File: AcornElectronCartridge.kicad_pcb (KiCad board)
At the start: 2 copper layers, 84.9 x 62.5 mm, 5 parts

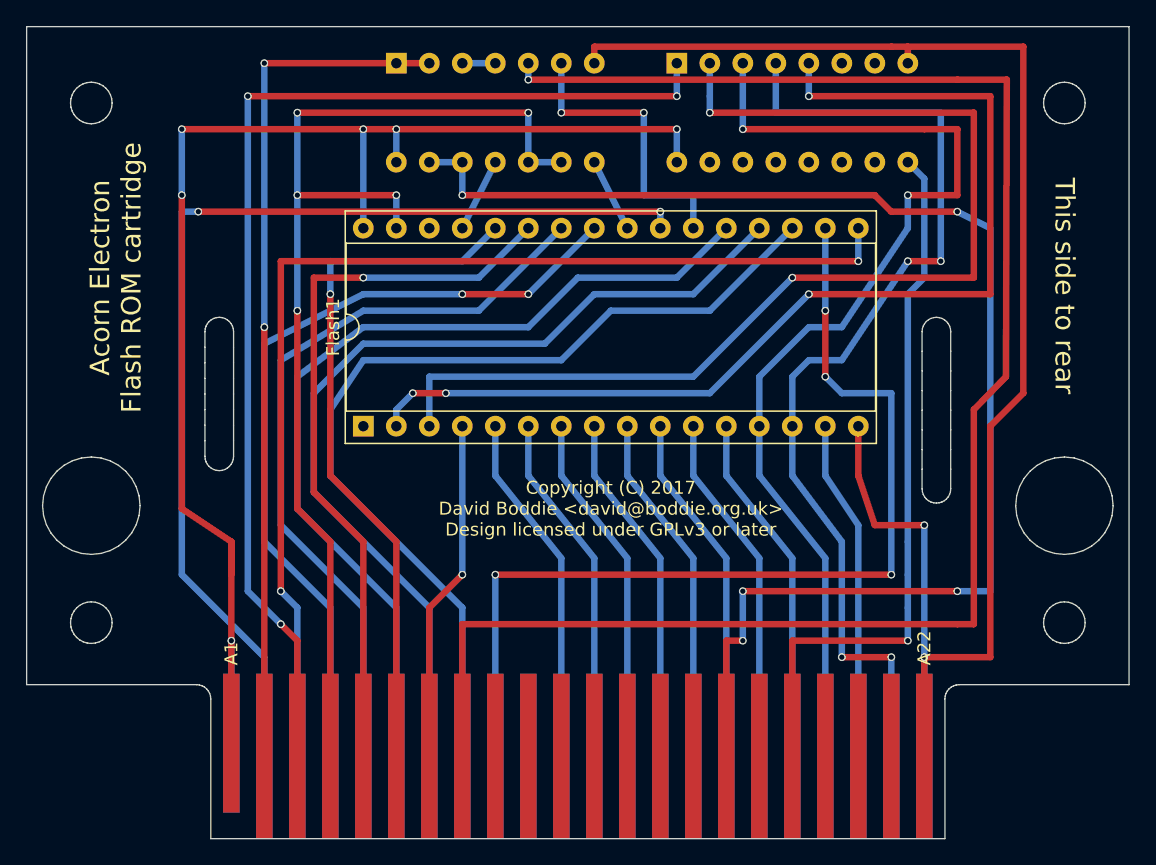
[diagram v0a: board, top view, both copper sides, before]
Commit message: Tidied up tracks to leave more space between silkscreen markings and vias. Only used one +5V line and kept the 0V lines separate.
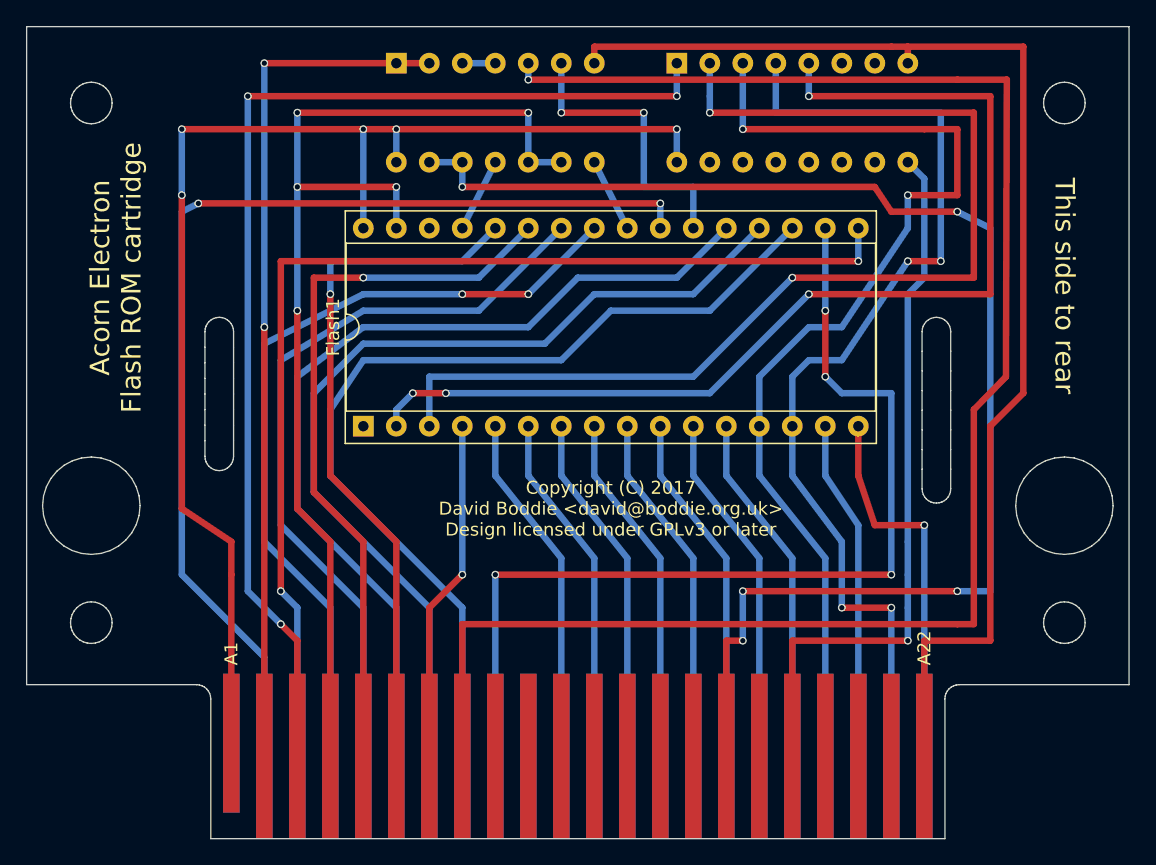
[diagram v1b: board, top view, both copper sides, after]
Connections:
- CONN2 pad 1: VCC -> /+5V_B
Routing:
- net VCC: track 110.5 -> 100.1 mm, vias 6 -> 5
- net /A10: track 82.6 -> 83.4 mm
- net /CSRW: track 84.9 -> 85.5 mm
- net GND: vias 2 -> 1

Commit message: Placed all tracks linked to flash ROM pads on the same side of the board.
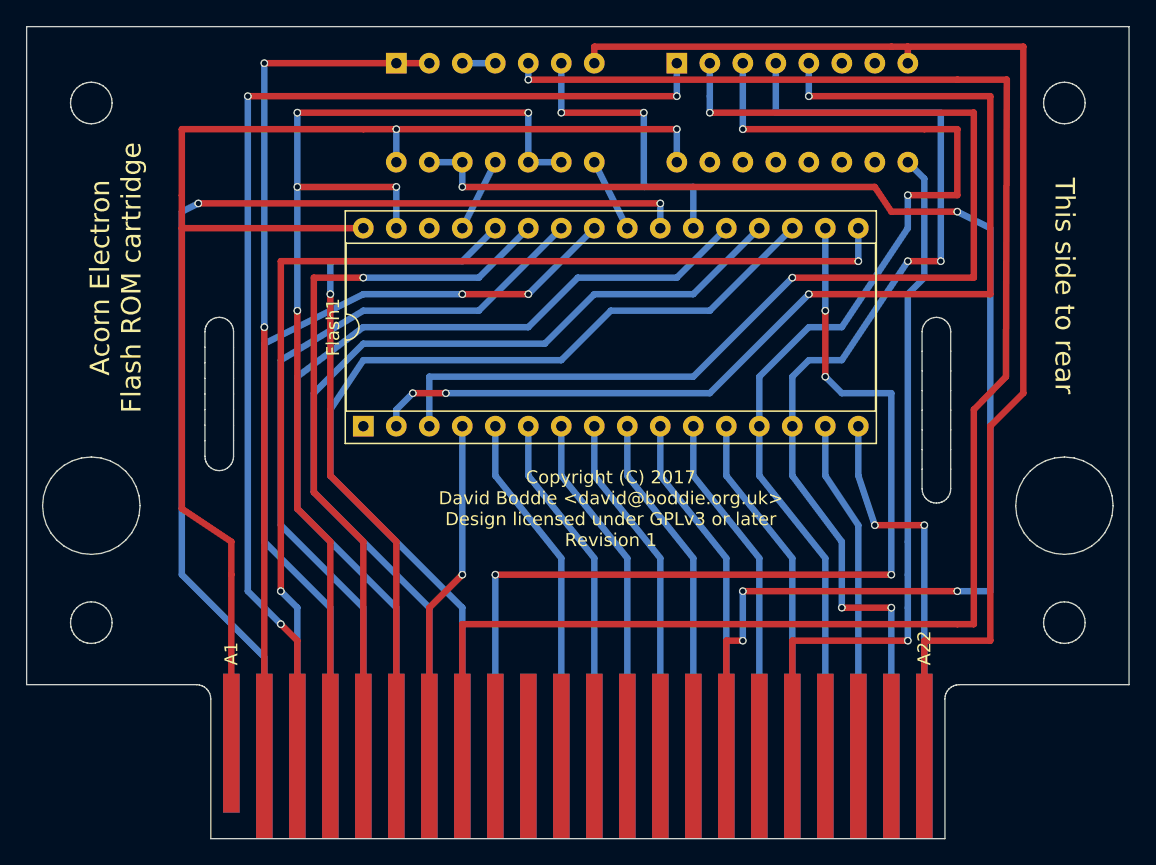
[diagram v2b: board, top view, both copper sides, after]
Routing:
- net VCC: track 100.1 -> 106.4 mm, vias 5 -> 2
- net GND: vias 1 -> 2
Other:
- board text added: "Copyright (C) 2017 David Boddie <david@boddie.org.uk> Design licensed under GPLv3 or later Revision 1"
- board text removed: "Copyright (C) 2017 David Boddie <david@boddie.org.uk> Design licensed under GPLv3 or later"
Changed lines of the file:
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@@
     (thickness 1.6)
     (drawings 322)
-    (tracks 295)
+    (tracks 294)
     (zones 0)
     (modules 5)
@@
     )
   )
-  (gr_text "Copyright (C) 2017\nDavid Boddie <david@boddie.org.uk>\nDesign licensed under GPLv3 or later" (at 105.41 101.6) (layer F.SilkS)
+  (gr_text "Copyright (C) 2017\nDavid Boddie <david@boddie.org.uk>\nDesign licensed under GPLv3 or later\nRevision 1" (at 105.41 101.6) (layer F.SilkS)
     (effects (font (size 1 1) (thickness 0.15)))
   )
@@
   (segment (start 119.38 99.06) (end 119.38 99.06) (width 0.5) (layer B.Cu) (net 39))
   (segment (start 119.38 99.06) (end 119.38 95.25) (width 0.5) (layer B.Cu) (net 39) (status 20))
+  (segment (start 86.36 80.01) (end 72.39 80.01) (width 0.5) (layer F.Cu) (net 41))
+  (segment (start 72.39 77.47) (end 72.39 72.39) (width 0.5) (layer F.Cu) (net 41))
+  (segment (start 86.36 72.39) (end 72.39 72.39) (width 0.5) (layer F.Cu) (net 41))
+  (segment (start 76.2 104.14) (end 72.39 101.6) (width 0.5) (layer F.Cu) (net 41))
+  (segment (start 72.39 101.6) (end 72.39 80.01) (width 0.5) (layer F.Cu) (net 41))
+  (segment (start 72.39 80.01) (end 72.39 77.47) (width 0.5) (layer F.Cu) (net 41))
+  (segment (start 76.2 104.14) (end 76.2 106.68) (width 0.5) (layer F.Cu) (net 41))
+  (segment (start 76.2 106.68) (end 76.2 119.65) (width 0.5) (layer F.Cu) (net 41))
   (segment (start 110.49 74.93) (end 110.49 72.39) (width 0.5) (layer B.Cu) (net 41) (status 10))
   (segment (start 110.49 72.39) (end 88.9 72.39) (width 0.5) (layer F.Cu) (net 41))
@@
   (segment (start 86.36 72.39) (end 88.9 72.39) (width 0.5) (layer F.Cu) (net 41))
   (segment (start 88.9 72.39) (end 88.9 74.93) (width 0.5) (layer B.Cu) (net 41) (status 20))
-  (via (at 72.39 77.47) (size 0.6) (drill 0.4) (layers F.Cu B.Cu) (net 41))
-  (segment (start 76.2 104.14) (end 72.39 101.6) (width 0.5) (layer F.Cu) (net 41))
-  (segment (start 72.39 101.6) (end 72.39 77.47) (width 0.5) (layer F.Cu) (net 41))
-  (segment (start 72.39 72.39) (end 86.36 72.39) (width 0.5) (layer F.Cu) (net 41))
-  (via (at 72.39 72.39) (size 0.6) (drill 0.4) (layers F.Cu B.Cu) (net 41))
-  (segment (start 72.39 77.47) (end 72.39 72.39) (width 0.5) (layer B.Cu) (net 41))
-  (segment (start 86.36 72.39) (end 86.36 80.01) (width 0.5) (layer B.Cu) (net 41) (status 20))
-  (segment (start 76.2 104.14) (end 76.2 106.68) (width 0.5) (layer F.Cu) (net 41))
-  (via (at 86.36 72.39) (size 0.6) (drill 0.4) (layers F.Cu B.Cu) (net 41))
-  (segment (start 76.2 119.65) (end 76.2 106.68) (width 0.5) (layer F.Cu) (net 41) (status 400000))
-  (segment (start 124.46 95.25) (end 124.46 99.06) (width 0.5) (layer F.Cu) (net 42) (status 10))
+  (segment (start 124.46 99.06) (end 124.46 95.25) (width 0.5) (layer B.Cu) (net 42))
+  (segment (start 125.73 102.87) (end 124.46 99.06) (width 0.5) (layer B.Cu) (net 42))
+  (via (at 125.73 102.87) (size 0.6) (drill 0.4) (layers F.Cu B.Cu) (net 42))
+  (segment (start 129.54 120.65) (end 129.54 113.03) (width 0.5) (layer B.Cu) (net 42) (status 10))
+  (segment (start 125.73 102.87) (end 129.54 102.87) (width 0.5) (layer F.Cu) (net 42))
+  (via (at 129.54 102.87) (size 0.6) (drill 0.4) (layers F.Cu B.Cu) (net 42))
   (segment (start 129.54 102.87) (end 129.54 113.03) (width 0.5) (layer B.Cu) (net 42))
-  (via (at 129.54 102.87) (size 0.6) (drill 0.4) (layers F.Cu B.Cu) (net 42))
-  (segment (start 125.73 102.87) (end 129.54 102.87) (width 0.5) (layer F.Cu) (net 42))
-  (segment (start 124.46 99.06) (end 125.73 102.87) (width 0.5) (layer F.Cu) (net 42))
-  (segment (start 134.62 95.25) (end 137.16 92.71) (width 0.5) (layer F.Cu) (net 42))
   (segment (start 128.27 66.04) (end 137.16 66.04) (width 0.5) (layer F.Cu) (net 42))
-  (segment (start 134.62 111.76) (end 129.54 111.76) (width 0.5) (layer F.Cu) (net 42))
-  (segment (start 134.62 111.76) (end 134.62 95.25) (width 0.5) (layer F.Cu) (net 42))
   (segment (start 137.16 92.71) (end 137.16 66.04) (width 0.5) (layer F.Cu) (net 42))
   (segment (start 127 66.04) (end 104.14 66.04) (width 0.5) (layer F.Cu) (net 42))
   (segment (start 104.14 66.04) (end 104.14 67.31) (width 0.5) (layer F.Cu) (net 42) (status 20))
   (segment (start 128.27 67.31) (end 128.27 66.04) (width 0.5) (layer F.Cu) (net 42) (status 10))
-  (segment (start 129.54 120.65) (end 129.54 113.03) (width 0.5) (layer B.Cu) (net 42) (status 10))
-  (segment (start 129.54 120.65) (end 129.54 111.76) (width 0.5) (layer F.Cu) (net 42) (status 10))
   (segment (start 128.27 66.04) (end 127 66.04) (width 0.5) (layer F.Cu) (net 42))
+  (segment (start 134.62 95.25) (end 137.16 92.71) (width 0.5) (layer F.Cu) (net 42))
+  (segment (start 134.62 111.76) (end 129.54 111.76) (width 0.5) (layer F.Cu) (net 42))
+  (segment (start 134.62 111.76) (end 134.62 95.25) (width 0.5) (layer F.Cu) (net 42))
+  (segment (start 129.54 120.65) (end 129.54 111.76) (width 0.5) (layer F.Cu) (net 42) (status 400010))
   (segment (start 106.68 80.01) (end 106.68 80.01) (width 0.5) (layer B.Cu) (net 43) (status 30))
   (segment (start 106.68 80.01) (end 104.14 74.93) (width 0.5) (layer B.Cu) (net 43) (status 30))

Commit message: Left more room between pads and tracks.
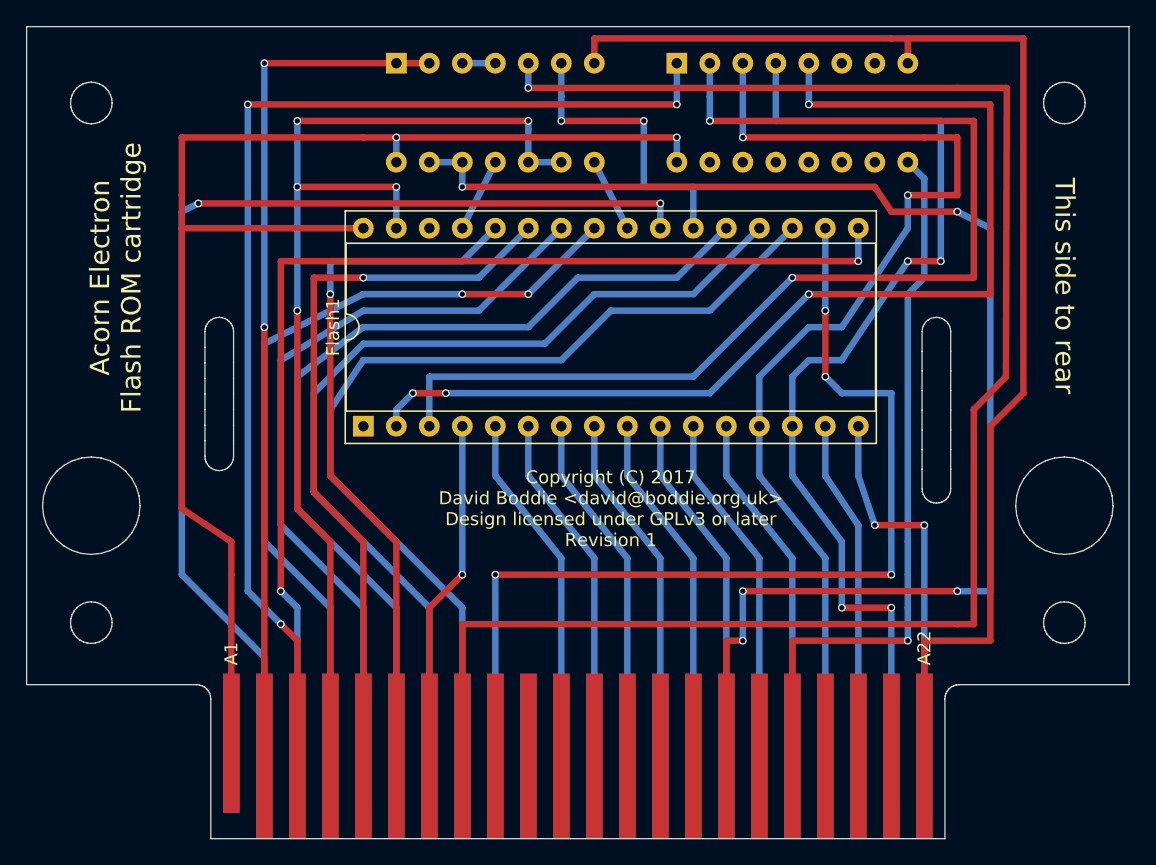
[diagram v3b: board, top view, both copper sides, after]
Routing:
- net VCC: track 106.4 -> 104.5 mm
- net GND: track 125.7 -> 127.6 mm
- net /CSRW: track 85.5 -> 84.2 mm

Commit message: Moved a via away from silkscreen text.
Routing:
- net /CE#: track 22.9 -> 20.6 mm
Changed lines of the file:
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@@
   )
   (segment (start 81.28 120.65) (end 81.28 111.76) (width 0.5) (layer F.Cu) (net 1) (status 10))
-  (segment (start 110.49 70.485) (end 110.49 67.31) (width 0.5) (layer B.Cu) (net 1) (status 800020))
+  (segment (start 110.49 70.485) (end 110.49 67.31) (width 0.5) (layer B.Cu) (net 1) (status 20))
   (via (at 110.49 70.485) (size 0.6) (drill 0.4) (layers F.Cu B.Cu) (net 1))
   (segment (start 77.47 70.485) (end 110.49 70.485) (width 0.5) (layer F.Cu) (net 1))
@@
   (segment (start 135.89 69.215) (end 132.08 69.215) (width 0.5) (layer F.Cu) (net 7))
   (via (at 99.06 69.215) (size 0.6) (drill 0.4) (layers F.Cu B.Cu) (net 7))
-  (segment (start 99.06 67.31) (end 99.06 69.215) (width 0.5) (layer B.Cu) (net 7) (status 400010))
+  (segment (start 99.06 67.31) (end 99.06 69.215) (width 0.5) (layer B.Cu) (net 7) (status 10))
   (segment (start 93.98 110.49) (end 132.08 110.49) (width 0.5) (layer F.Cu) (net 7))
   (segment (start 93.98 110.49) (end 93.98 120.65) (width 0.5) (layer F.Cu) (net 7) (status 20))
@@
   (segment (start 123.19 87.63) (end 128.27 80.01) (width 0.5) (layer B.Cu) (net 37))
   (segment (start 132.08 77.47) (end 132.08 73.025) (width 0.5) (layer F.Cu) (net 37))
-  (segment (start 115.57 67.31) (end 115.57 73.025) (width 0.5) (layer B.Cu) (net 37) (status 400010))
+  (segment (start 115.57 67.31) (end 115.57 73.025) (width 0.5) (layer B.Cu) (net 37) (status 10))
   (via (at 115.57 73.025) (size 0.6) (drill 0.4) (layers F.Cu B.Cu) (net 37))
   (segment (start 132.08 73.025) (end 129.54 73.025) (width 0.5) (layer F.Cu) (net 37))
@@
   (segment (start 130.81 82.55) (end 130.81 71.755) (width 0.5) (layer B.Cu) (net 39))
   (segment (start 130.81 71.755) (end 118.11 71.755) (width 0.5) (layer B.Cu) (net 39))
-  (segment (start 118.11 67.31) (end 118.11 71.755) (width 0.5) (layer B.Cu) (net 39) (status 400010))
+  (segment (start 118.11 67.31) (end 118.11 71.755) (width 0.5) (layer B.Cu) (net 39) (status 10))
   (segment (start 119.38 91.44) (end 119.38 95.25) (width 0.5) (layer B.Cu) (net 39) (status 20))
   (segment (start 127 120.65) (end 127 109.22) (width 0.5) (layer B.Cu) (net 39) (status 10))
@@
   (segment (start 76.2 104.14) (end 76.2 106.68) (width 0.5) (layer F.Cu) (net 41))
   (segment (start 76.2 106.68) (end 76.2 119.65) (width 0.5) (layer F.Cu) (net 41))
-  (segment (start 110.49 74.93) (end 110.49 73.025) (width 0.5) (layer B.Cu) (net 41) (status 400010))
+  (segment (start 110.49 74.93) (end 110.49 73.025) (width 0.5) (layer B.Cu) (net 41) (status 10))
   (segment (start 110.49 73.025) (end 88.9 73.025) (width 0.5) (layer F.Cu) (net 41))
   (via (at 110.49 73.025) (size 0.6) (drill 0.4) (layers F.Cu B.Cu) (net 41))
   (via (at 88.9 73.025) (size 0.6) (drill 0.4) (layers F.Cu B.Cu) (net 41))
   (segment (start 86.36 73.025) (end 88.9 73.025) (width 0.5) (layer F.Cu) (net 41))
-  (segment (start 88.9 73.025) (end 88.9 74.93) (width 0.5) (layer B.Cu) (net 41) (status 800020))
+  (segment (start 88.9 73.025) (end 88.9 74.93) (width 0.5) (layer B.Cu) (net 41) (status 20))
   (segment (start 124.46 99.06) (end 124.46 95.25) (width 0.5) (layer B.Cu) (net 42))
   (segment (start 125.73 102.87) (end 124.46 99.06) (width 0.5) (layer B.Cu) (net 42))
@@
   (segment (start 101.6 69.85) (end 101.6 71.755) (width 0.5) (layer B.Cu) (net 46))
   (via (at 101.6 71.755) (size 0.6) (drill 0.4) (layers F.Cu B.Cu) (net 46))
-  (segment (start 101.6 71.755) (end 107.95 71.755) (width 0.5) (layer F.Cu) (net 46))
-  (via (at 107.95 71.755) (size 0.6) (drill 0.4) (layers F.Cu B.Cu) (net 46))
-  (segment (start 107.95 71.755) (end 107.95 76.835) (width 0.5) (layer B.Cu) (net 46))
+  (segment (start 101.6 71.755) (end 104.775 71.755) (width 0.5) (layer F.Cu) (net 46))
+  (via (at 104.775 71.755) (size 0.6) (drill 0.4) (layers F.Cu B.Cu) (net 46))
+  (segment (start 104.775 71.755) (end 107.95 76.835) (width 0.5) (layer B.Cu) (net 46))
   (segment (start 107.95 76.835) (end 111.76 76.835) (width 0.5) (layer B.Cu) (net 46))
   (segment (start 101.6 69.85) (end 101.6 67.31) (width 0.5) (layer B.Cu) (net 46) (status 20))
@@
   (segment (start 88.9 95.25) (end 88.9 93.98) (width 0.5) (layer B.Cu) (net 53) (status 10))
   (segment (start 134.62 85.09) (end 134.62 70.485) (width 0.5) (layer F.Cu) (net 53))
-  (segment (start 120.65 70.485) (end 120.65 67.31) (width 0.5) (layer B.Cu) (net 53) (status 800020))
+  (segment (start 120.65 70.485) (end 120.65 67.31) (width 0.5) (layer B.Cu) (net 53) (status 20))
   (via (at 120.65 70.485) (size 0.6) (drill 0.4) (layers F.Cu B.Cu) (net 53))
   (segment (start 134.62 70.485) (end 120.65 70.485) (width 0.5) (layer F.Cu) (net 53))

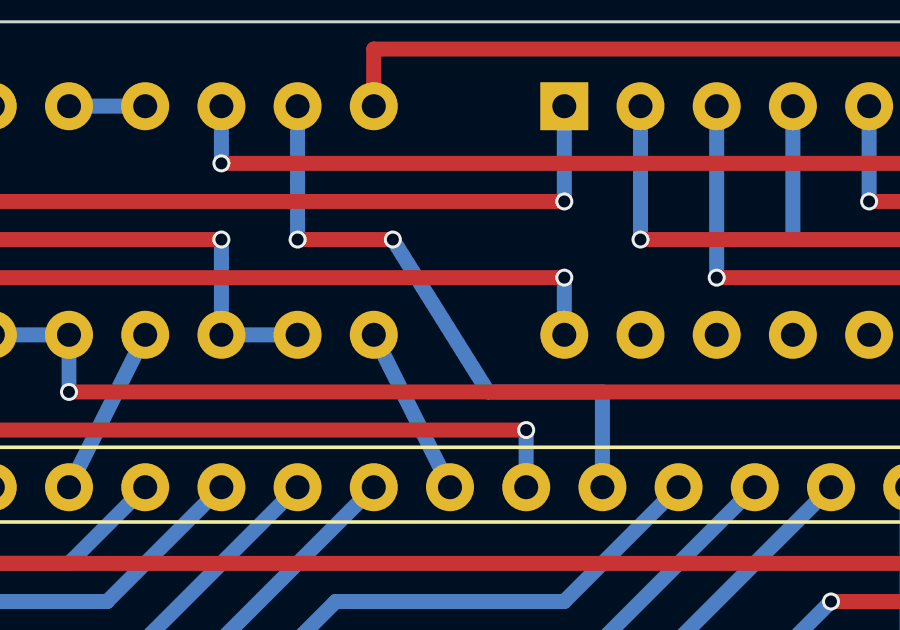
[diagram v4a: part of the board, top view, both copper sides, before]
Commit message: Tweaking a via position.
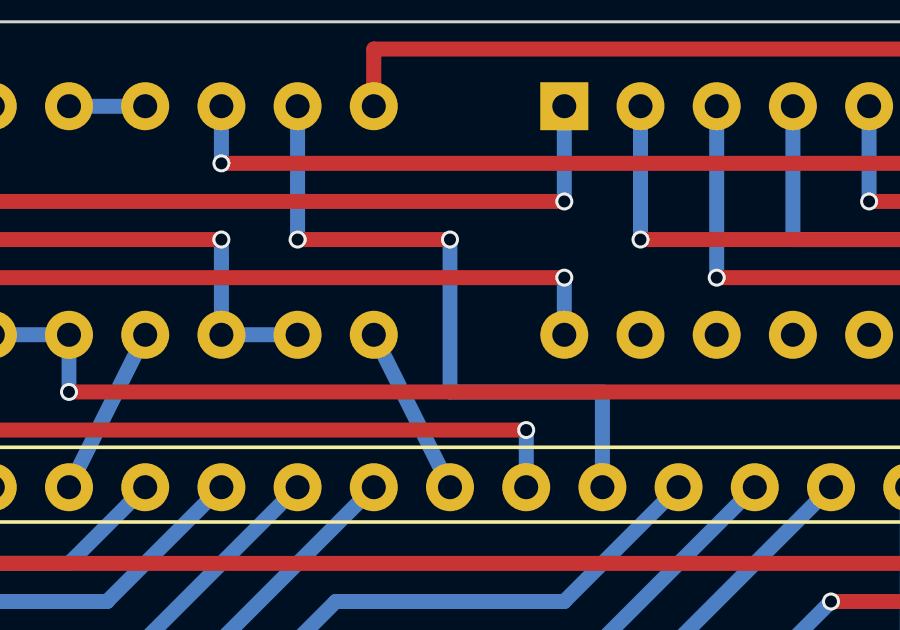
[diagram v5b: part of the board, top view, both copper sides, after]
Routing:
- net /CE#: track 20.6 -> 22.9 mm
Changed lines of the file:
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@@
   (segment (start 101.6 69.85) (end 101.6 71.755) (width 0.5) (layer B.Cu) (net 46))
   (via (at 101.6 71.755) (size 0.6) (drill 0.4) (layers F.Cu B.Cu) (net 46))
-  (segment (start 101.6 71.755) (end 104.775 71.755) (width 0.5) (layer F.Cu) (net 46))
-  (via (at 104.775 71.755) (size 0.6) (drill 0.4) (layers F.Cu B.Cu) (net 46))
-  (segment (start 104.775 71.755) (end 107.95 76.835) (width 0.5) (layer B.Cu) (net 46))
-  (segment (start 107.95 76.835) (end 111.76 76.835) (width 0.5) (layer B.Cu) (net 46))
+  (segment (start 101.6 71.755) (end 106.68 71.755) (width 0.5) (layer F.Cu) (net 46))
+  (via (at 106.68 71.755) (size 0.6) (drill 0.4) (layers F.Cu B.Cu) (net 46))
+  (segment (start 106.68 71.755) (end 106.68 76.835) (width 0.5) (layer B.Cu) (net 46))
+  (segment (start 106.68 76.835) (end 111.76 76.835) (width 0.5) (layer B.Cu) (net 46))
   (segment (start 101.6 69.85) (end 101.6 67.31) (width 0.5) (layer B.Cu) (net 46) (status 20))
   (segment (start 101.6 67.31) (end 101.6 67.31) (width 0.5) (layer B.Cu) (net 46) (status 30))
